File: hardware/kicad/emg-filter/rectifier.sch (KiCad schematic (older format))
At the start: 80 parts, among them U35 LM4565, U36 LM4565, U37 LM4565, U38 LM4565, U39 LM4565, U40 LM4565, U41 LM4565, U42 LM4565

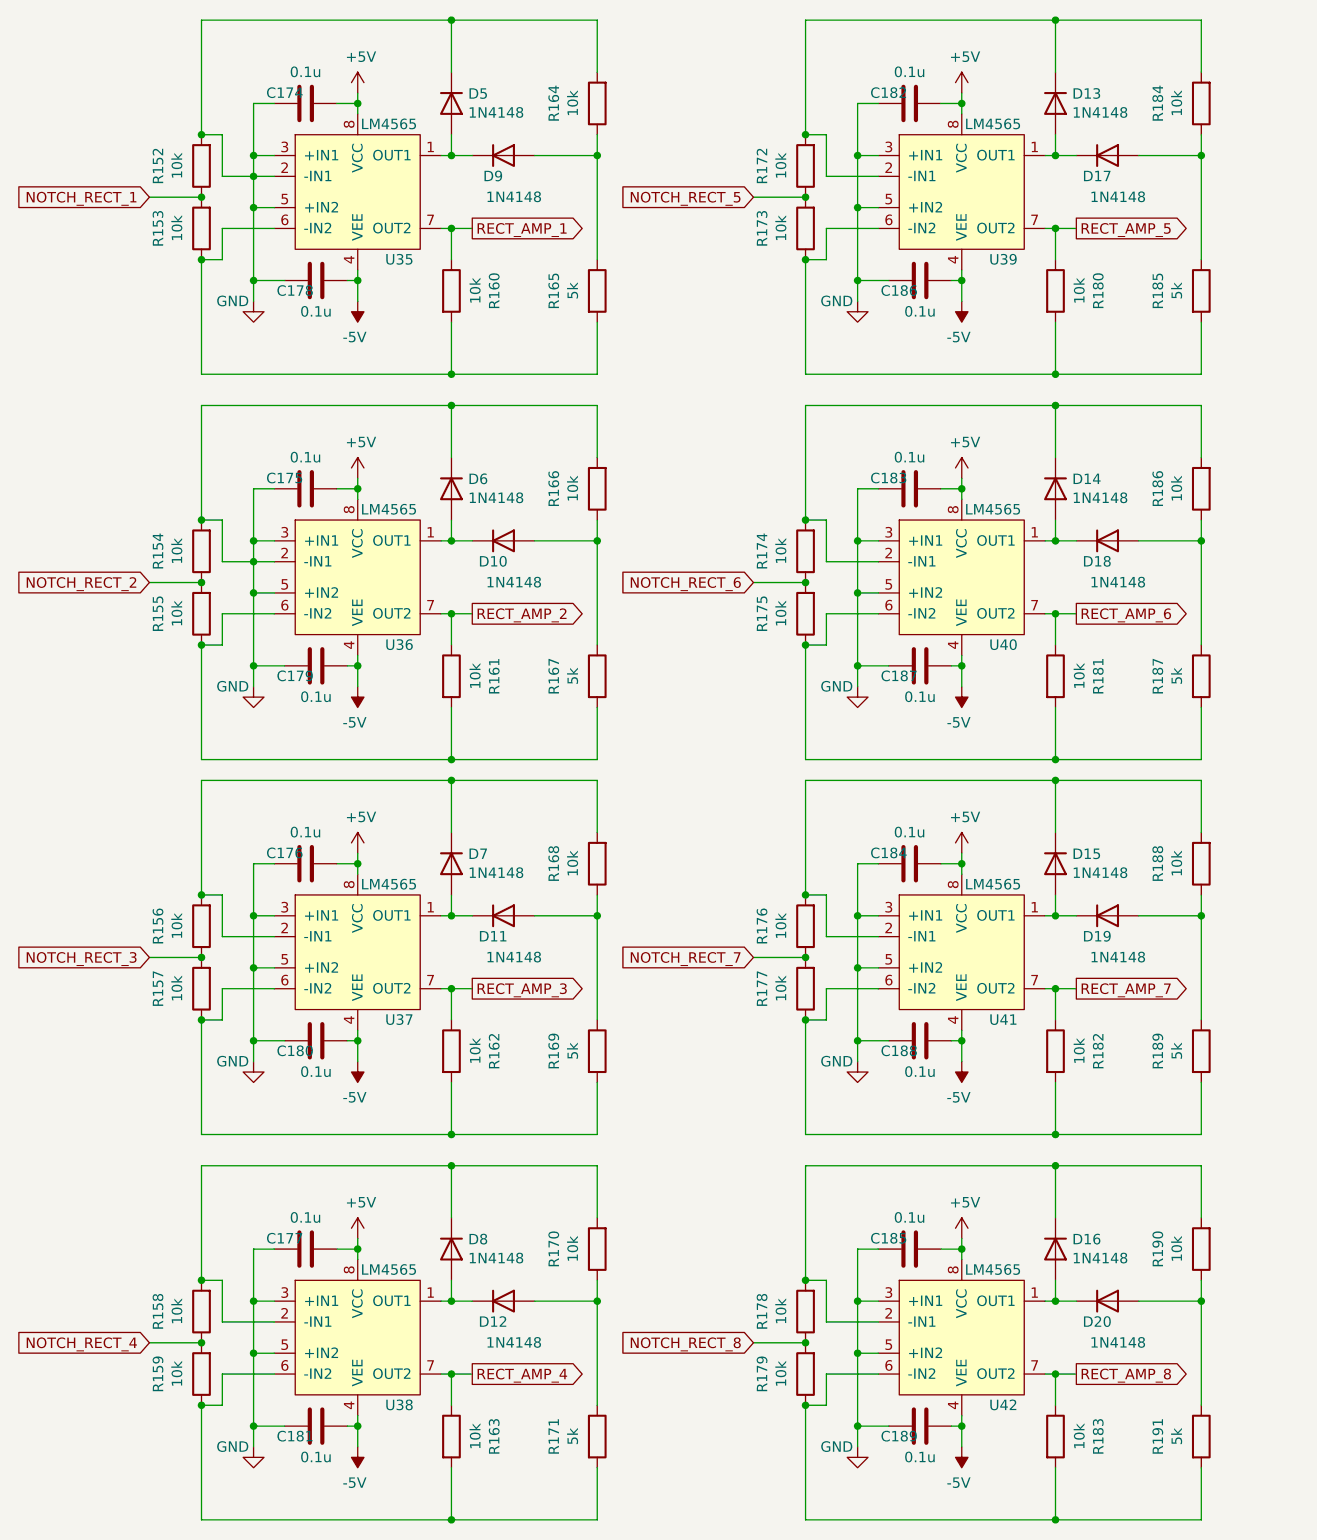
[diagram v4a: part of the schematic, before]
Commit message: footprint association
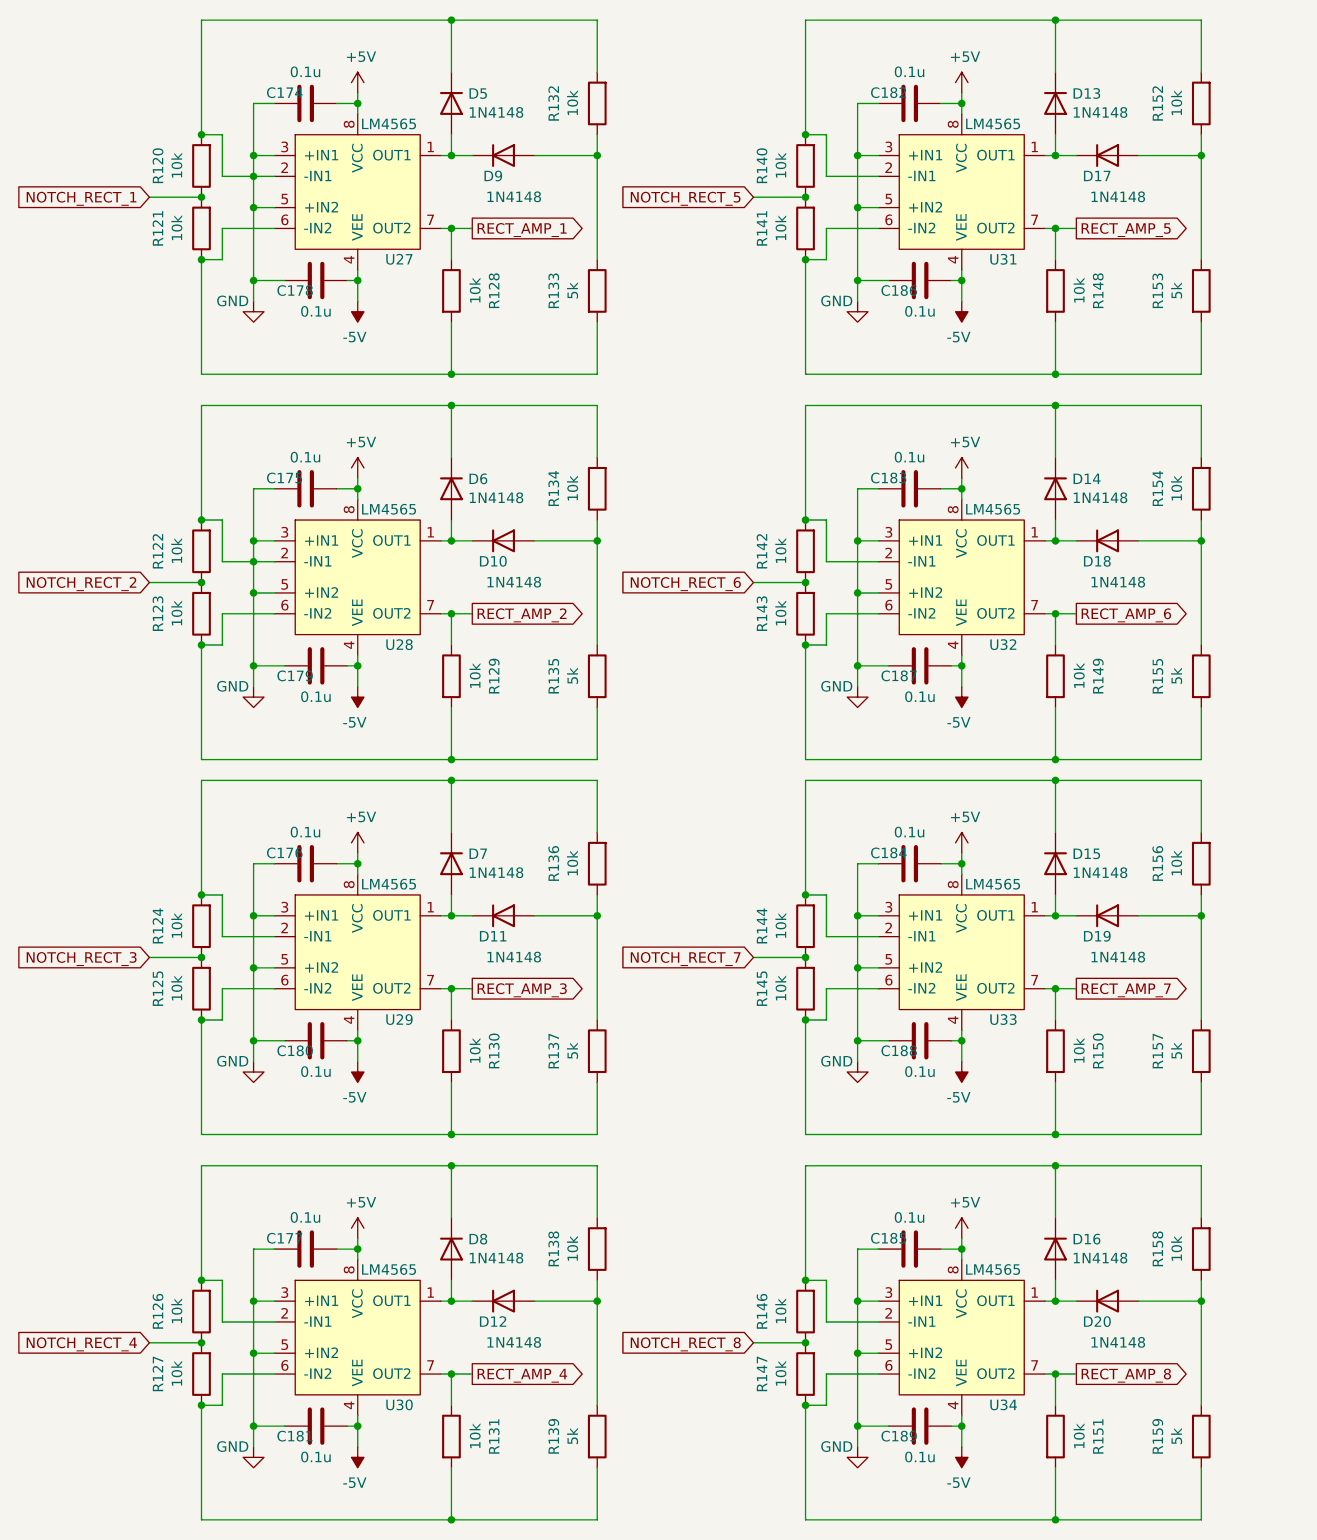
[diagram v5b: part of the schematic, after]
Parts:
- C174, C175, C176, C177, C178, C179, C180, C181, C182, C183, C184, C185, C186, C187, C188, C189: footprint (none) -> Capacitor_SMD:C_0805_2012Metric
- D10, D11, D12, D13, D14, D15, D16, D17, D18, D19, D20, D5, D6, D7, D8, D9: footprint (none) -> Diode_SMD:D_SOD-323
- R120: renamed from R152; footprint (none) -> Resistor_SMD:R_0805_2012Metric
- R121: renamed from R153; footprint (none) -> Resistor_SMD:R_0805_2012Metric
- R122: renamed from R154; footprint (none) -> Resistor_SMD:R_0805_2012Metric
- R123: renamed from R155; footprint (none) -> Resistor_SMD:R_0805_2012Metric
- R124: renamed from R156; footprint (none) -> Resistor_SMD:R_0805_2012Metric
- R125: renamed from R157; footprint (none) -> Resistor_SMD:R_0805_2012Metric
- R126: renamed from R158; footprint (none) -> Resistor_SMD:R_0805_2012Metric
- R127: renamed from R159; footprint (none) -> Resistor_SMD:R_0805_2012Metric
- R128: renamed from R160; footprint (none) -> Resistor_SMD:R_0805_2012Metric
- R129: renamed from R161; footprint (none) -> Resistor_SMD:R_0805_2012Metric
- R130: renamed from R162; footprint (none) -> Resistor_SMD:R_0805_2012Metric
- R131: renamed from R163; footprint (none) -> Resistor_SMD:R_0805_2012Metric
- R132: renamed from R164; footprint (none) -> Resistor_SMD:R_0805_2012Metric
- R133: renamed from R165; footprint (none) -> Resistor_SMD:R_0805_2012Metric
- R134: renamed from R166; footprint (none) -> Resistor_SMD:R_0805_2012Metric
- R135: renamed from R167; footprint (none) -> Resistor_SMD:R_0805_2012Metric
- R136: renamed from R168; footprint (none) -> Resistor_SMD:R_0805_2012Metric
- R137: renamed from R169; footprint (none) -> Resistor_SMD:R_0805_2012Metric
- R138: renamed from R170; footprint (none) -> Resistor_SMD:R_0805_2012Metric
- R139: renamed from R171; footprint (none) -> Resistor_SMD:R_0805_2012Metric
- R140: renamed from R172; footprint (none) -> Resistor_SMD:R_0805_2012Metric
- R141: renamed from R173; footprint (none) -> Resistor_SMD:R_0805_2012Metric
- R142: renamed from R174; footprint (none) -> Resistor_SMD:R_0805_2012Metric
- R143: renamed from R175; footprint (none) -> Resistor_SMD:R_0805_2012Metric
- R144: renamed from R176; footprint (none) -> Resistor_SMD:R_0805_2012Metric
- R145: renamed from R177; footprint (none) -> Resistor_SMD:R_0805_2012Metric
- R146: renamed from R178; footprint (none) -> Resistor_SMD:R_0805_2012Metric
- R147: renamed from R179; footprint (none) -> Resistor_SMD:R_0805_2012Metric
- R148: renamed from R180; footprint (none) -> Resistor_SMD:R_0805_2012Metric
- R149: renamed from R181; footprint (none) -> Resistor_SMD:R_0805_2012Metric
- R150: renamed from R182; footprint (none) -> Resistor_SMD:R_0805_2012Metric
- R151: renamed from R183; footprint (none) -> Resistor_SMD:R_0805_2012Metric
- R152: renamed from R184; footprint (none) -> Resistor_SMD:R_0805_2012Metric
- R153: renamed from R185; footprint (none) -> Resistor_SMD:R_0805_2012Metric
- R154: renamed from R186; footprint (none) -> Resistor_SMD:R_0805_2012Metric
- R155: renamed from R187; footprint (none) -> Resistor_SMD:R_0805_2012Metric
- R156: renamed from R188; footprint (none) -> Resistor_SMD:R_0805_2012Metric
- R157: renamed from R189; footprint (none) -> Resistor_SMD:R_0805_2012Metric
- R158: renamed from R190; footprint (none) -> Resistor_SMD:R_0805_2012Metric
- R159: renamed from R191; footprint (none) -> Resistor_SMD:R_0805_2012Metric
- renumbered U35 to U27, U36 to U28, U37 to U29, U38 to U30, U39 to U31, U40 to U32, U41 to U33, U42 to U34

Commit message: Solving Stuff for Free
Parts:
- renumbered R120 to R152, R121 to R153, R122 to R154, R123 to R155, R124 to R156, R125 to R157, R126 to R158, R127 to R159, R128 to R160, R129 to R161, R130 to R162, R131 to R163, R132 to R164, R133 to R165, R134 to R166, R135 to R167, R136 to R168, R137 to R169, R138 to R170, R139 to R171, R140 to R172, R141 to R173, R142 to R174, R143 to R175, R144 to R176, R145 to R177, R146 to R178, R147 to R179, R148 to R180, R149 to R181, R150 to R182, R151 to R183, R152 to R184, R153 to R185, R154 to R186, R155 to R187, R156 to R188, R157 to R189, R158 to R190, R159 to R191

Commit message: pcb
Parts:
- U27, U28, U29, U30, U31, U32, U33, U34: footprint (none) -> emg-filter:LM4565
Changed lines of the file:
@@
 F 0 "U34" H 5250 6500 50  0000 C CNN
 F 1 "LM4565" H 5200 7150 50  0000 C CNN
-F 2 "" H 6050 6850 50  0001 C CNN
+F 2 "emg-filter:LM4565" H 6050 6850 50  0001 C CNN
 F 3 "" H 6050 6850 50  0001 C CNN
 	1    5050 6850
@@
 F 0 "U33" H 5250 4650 50  0000 C CNN
 F 1 "LM4565" H 5200 5300 50  0000 C CNN
-F 2 "" H 6050 5000 50  0001 C CNN
+F 2 "emg-filter:LM4565" H 6050 5000 50  0001 C CNN
 F 3 "" H 6050 5000 50  0001 C CNN
 	1    5050 5000
@@
 F 0 "U32" H 5250 2850 50  0000 C CNN
 F 1 "LM4565" H 5200 3500 50  0000 C CNN
-F 2 "" H 6050 3200 50  0001 C CNN
+F 2 "emg-filter:LM4565" H 6050 3200 50  0001 C CNN
 F 3 "" H 6050 3200 50  0001 C CNN
 	1    5050 3200
@@
 F 0 "U31" H 5250 1000 50  0000 C CNN
 F 1 "LM4565" H 5200 1650 50  0000 C CNN
-F 2 "" H 6050 1350 50  0001 C CNN
+F 2 "emg-filter:LM4565" H 6050 1350 50  0001 C CNN
 F 3 "" H 6050 1350 50  0001 C CNN
 	1    5050 1350
@@
 F 0 "U30" H 2350 6500 50  0000 C CNN
 F 1 "LM4565" H 2300 7150 50  0000 C CNN
-F 2 "" H 3150 6850 50  0001 C CNN
+F 2 "emg-filter:LM4565" H 3150 6850 50  0001 C CNN
 F 3 "" H 3150 6850 50  0001 C CNN
 	1    2150 6850
@@
 F 0 "U29" H 2350 4650 50  0000 C CNN
 F 1 "LM4565" H 2300 5300 50  0000 C CNN
-F 2 "" H 3150 5000 50  0001 C CNN
+F 2 "emg-filter:LM4565" H 3150 5000 50  0001 C CNN
 F 3 "" H 3150 5000 50  0001 C CNN
 	1    2150 5000
@@
 F 0 "U28" H 2350 2850 50  0000 C CNN
 F 1 "LM4565" H 2300 3500 50  0000 C CNN
-F 2 "" H 3150 3200 50  0001 C CNN
+F 2 "emg-filter:LM4565" H 3150 3200 50  0001 C CNN
 F 3 "" H 3150 3200 50  0001 C CNN
 	1    2150 3200
@@
 F 0 "U27" H 2350 1000 50  0000 C CNN
 F 1 "LM4565" H 2300 1650 50  0000 C CNN
-F 2 "" H 3150 1350 50  0001 C CNN
+F 2 "emg-filter:LM4565" H 3150 1350 50  0001 C CNN
 F 3 "" H 3150 1350 50  0001 C CNN
 	1    2150 1350
